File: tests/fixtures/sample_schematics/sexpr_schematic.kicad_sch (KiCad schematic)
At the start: 2 parts

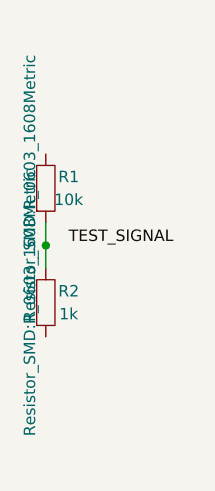
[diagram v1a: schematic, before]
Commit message: feat: implement wire connectivity tracing in netlist builder (#62)
## Summary

Closes #56

- Replace the stubbed `_build_netlist()` with a Union-Find based
`ConnectivityEngine` that traces wire segments, junctions, labels, and
component pins to build accurate netlists from KiCad schematics
- Add pin position resolution from `lib_symbols` section with rotation
support (0/90/180/270 degrees)
- Fix label extraction regex that failed on deeply nested S-expressions
(3+ levels of parens)
- Update `parse_json_schematic()` to use `ConnectivityEngine` as
fallback when explicit nets are missing, and fill in labels/junctions
TODOs
- Fix dangling label position in test fixture (was 2.54mm off from wire
endpoint)

### New files
- `kicad_mcp/utils/connectivity.py` — `UnionFind`, `quantize_point`,
`ConnectivityEngine`
- `tests/unit/utils/test_connectivity.py` — 26 unit tests

### Modified files
- `kicad_mcp/utils/netlist_parser.py` — new methods
`_extract_lib_symbol_pins()`, `_resolve_pin_positions()`, replaced
`_build_netlist()`, fixed `_extract_labels()`, updated
`parse_json_schematic()`
- `tests/unit/utils/test_netlist_parser.py` — 8 new integration tests in
`TestBuildNetlist`
- `tests/fixtures/sample_schematics/sexpr_schematic.kicad_sch` — label
position fix

### Known limitations (documented, not in scope)
- Mirrored components (`mirror x/y`) not handled
- Multi-unit symbols (e.g., op-amps) not handled
- Hierarchical sheet cross-sheet connectivity not implemented

## Test plan

- [x] 56 new tests pass (26 connectivity unit + 8 parser integration +
22 existing)
- [x] Full suite: 393 passed, 1 pre-existing failure (macOS sandbox), 2
pre-existing skips
- [x] Coverage increased from 39% to 41.89%
- [x] Verified R1.pin2 + R2.pin1 correctly placed in `TEST_SIGNAL` net
via wire chain

🤖 Generated with [Claude Code](https://claude.com/claude-code)

Co-authored-by: Claude Opus 4.6 <noreply@anthropic.com>
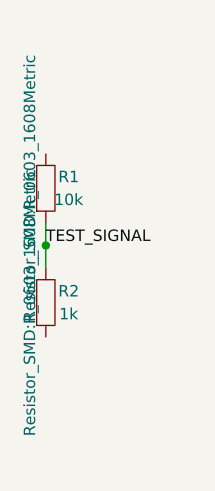
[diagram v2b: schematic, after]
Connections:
- net TEST_SIGNAL: now also R1.2, R2.1
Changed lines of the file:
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@@
     (uuid "wire-uuid-5678")
   )
-  (label "TEST_SIGNAL" (at 66.04 93.98 0) (fields_autoplaced)
+  (label "TEST_SIGNAL" (at 63.5 93.98 0) (fields_autoplaced)
     (effects (font (size 1.27 1.27)) (justify left bottom))
     (uuid "label-uuid-1234")
